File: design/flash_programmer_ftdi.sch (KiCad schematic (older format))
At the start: 13 parts, among them P201 USB_B, U201 FT230X

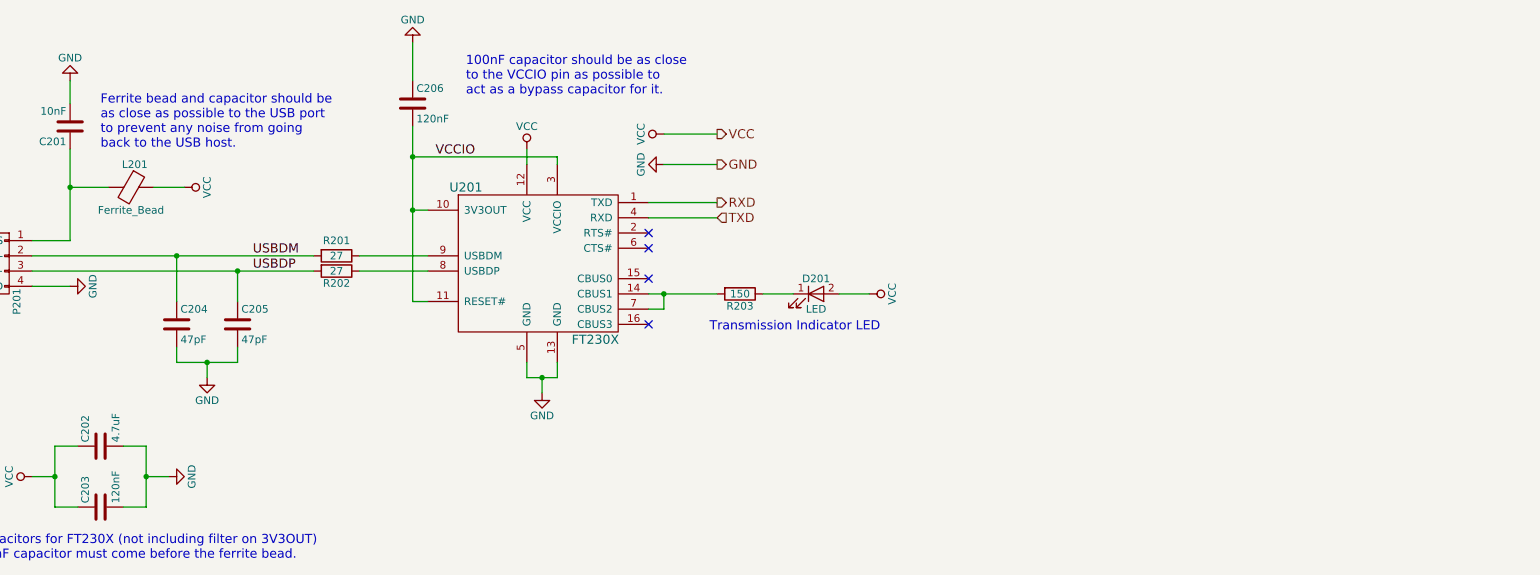
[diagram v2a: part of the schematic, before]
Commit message: Redraw schematic for clarity
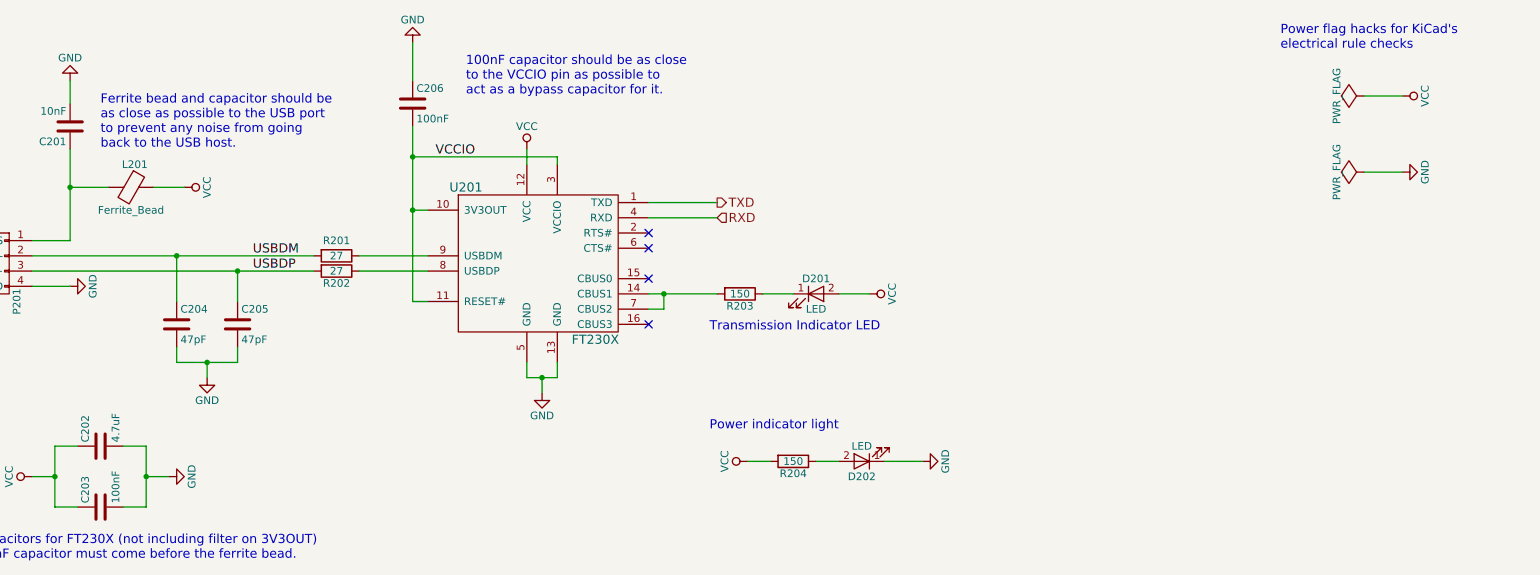
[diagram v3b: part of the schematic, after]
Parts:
- added D202: LED, LEDs:LED_0805, symbol LED
- added R204: 150, Resistors_SMD:R_0805_HandSoldering, symbol R
- C203, C206: value 120nF -> 100nF
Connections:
- net GND: now also D202.1 (K)
- net RXD: now also U201.4 (RXD); no longer U201.1 (TXD)
- net TXD: now also U201.1 (TXD); no longer U201.4 (RXD)
- net VCC: now also R204.2
- new net: D202.2 (A), R204.1
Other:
- note added: "Power flag hacks for KiCad's\nelectrical rule checks"
- note added: "Power indicator light"
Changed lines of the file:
@@
 EESchema Schematic File Version 2
+LIBS:gls27sf010
 LIBS:flash_programmer
 LIBS:power
@@
 $Descr A4 11693 8268
 encoding utf-8
-Sheet 2 3
+Sheet 2 4
 Title ""
 Date ""
@@
 $EndDescr
 $Comp
-L VCC #PWR028
+L VCC #PWR01
 U 1 1 58666138
 P 2500 1700
-F 0 "#PWR028" H 2500 1550 50  0001 C CNN
+F 0 "#PWR01" H 2500 1550 50  0001 C CNN
 F 1 "VCC" H 2500 1850 50  0000 C CNN
 F 2 "" H 2500 1700 50  0000 C CNN
@@
 $EndComp
 $Comp
-L GND #PWR029
+L GND #PWR02
 U 1 1 58666150
 P 1750 1000
-F 0 "#PWR029" H 1750 750 50  0001 C CNN
+F 0 "#PWR02" H 1750 750 50  0001 C CNN
 F 1 "GND" H 1750 850 50  0000 C CNN
 F 2 "" H 1750 1000 50  0000 C CNN
@@
 P 1950 3800
 F 0 "C203" H 1975 3900 50  0000 L CNN
-F 1 "120nF" H 1975 3700 50  0000 L CNN
+F 1 "100nF" H 1975 3700 50  0000 L CNN
 F 2 "Capacitors_SMD:C_0805_HandSoldering" H 1988 3650 50  0001 C CNN
 F 3 "" H 1950 3800 50  0000 C CNN
@@
 P 4000 1150
 F 0 "C206" H 4025 1250 50  0000 L CNN
-F 1 "120nF" H 4025 1050 50  0000 L CNN
+F 1 "100nF" H 4025 1050 50  0000 L CNN
 F 2 "Capacitors_SMD:C_0805_HandSoldering" H 4038 1000 50  0001 C CNN
 F 3 "" H 4000 1150 50  0000 C CNN
@@
 	1650 3400 1800 3400
 $Comp
-L GND #PWR030
+L GND #PWR03
 U 1 1 58666A15
 P 2400 3600
-F 0 "#PWR030" H 2400 3350 50  0001 C CNN
+F 0 "#PWR03" H 2400 3350 50  0001 C CNN
 F 1 "GND" H 2400 3450 50  0000 C CNN
 F 2 "" H 2400 3600 50  0000 C CNN
@@
 $EndComp
 $Comp
-L VCC #PWR031
+L VCC #PWR04
 U 1 1 58666A32
 P 1500 3600
-F 0 "#PWR031" H 1500 3450 50  0001 C CNN
+F 0 "#PWR04" H 1500 3450 50  0001 C CNN
 F 1 "VCC" H 1500 3750 50  0000 C CNN
 F 2 "" H 1500 3600 50  0000 C CNN
@@
 $EndComp
 $Comp
-L GND #PWR032
+L GND #PWR05
 U 1 1 58667B03
 P 4850 3050
-F 0 "#PWR032" H 4850 2800 50  0001 C CNN
+F 0 "#PWR05" H 4850 2800 50  0001 C CNN
 F 1 "GND" H 4850 2900 50  0000 C CNN
 F 2 "" H 4850 3050 50  0000 C CNN
@@
 	2300 1700 2500 1700
 $Comp
-L GND #PWR033
+L GND #PWR06
 U 1 1 58669DB0
 P 1750 2350
-F 0 "#PWR033" H 1750 2100 50  0001 C CNN
+F 0 "#PWR06" H 1750 2100 50  0001 C CNN
 F 1 "GND" H 1750 2200 50  0000 C CNN
 F 2 "" H 1750 2350 50  0000 C CNN
@@
 	4750 1550 4750 1450
 $Comp
-L VCC #PWR034
+L VCC #PWR07
 U 1 1 5867040E
 P 4750 1450
-F 0 "#PWR034" H 4750 1300 50  0001 C CNN
+F 0 "#PWR07" H 4750 1300 50  0001 C CNN
 F 1 "VCC" H 4750 1600 50  0000 C CNN
 F 2 "" H 4750 1450 50  0000 C CNN
@@
 	4000 1000 4000 750
 $Comp
-L GND #PWR035
+L GND #PWR08
 U 1 1 58670F4A
 P 4000 750
-F 0 "#PWR035" H 4000 500 50  0001 C CNN
+F 0 "#PWR08" H 4000 500 50  0001 C CNN
 F 1 "GND" H 4000 600 50  0000 C CNN
 F 2 "" H 4000 750 50  0000 C CNN
@@
 NoConn ~ 5550 2000
 NoConn ~ 5550 2100
-Wire Wire Line
-	5550 1800 6000 1800
-Wire Wire Line
-	5550 1900 6000 1900
 $Comp
 L R R202
@@
 Connection ~ 2650 2850
 $Comp
-L GND #PWR036
+L GND #PWR09
 U 1 1 58674AD8
 P 2650 2950
-F 0 "#PWR036" H 2650 2700 50  0001 C CNN
+F 0 "#PWR09" H 2650 2700 50  0001 C CNN
 F 1 "GND" H 2650 2800 50  0000 C CNN
 F 2 "" H 2650 2950 50  0000 C CNN
@@
 Wire Wire Line
 	6500 2400 6300 2400
+Text HLabel 6000 1900 2    60   Input ~ 0
+RXD
 Text HLabel 6000 1800 2    60   Output ~ 0
-RXD
-Text HLabel 6000 1900 2    60   Input ~ 0
 TXD
-Wire Wire Line
-	5650 1550 6000 1550
-Wire Wire Line
-	5650 1350 6000 1350
-$Comp
-L VCC #PWR037
-U 1 1 5867D289
-P 5650 1350
-F 0 "#PWR037" H 5650 1200 50  0001 C CNN
-F 1 "VCC" H 5650 1500 50  0000 C CNN
-F 2 "" H 5650 1350 50  0000 C CNN
-F 3 "" H 5650 1350 50  0000 C CNN
-	1    5650 1350
-	0    -1   -1   0
-$EndComp
-$Comp
-L GND #PWR038
-U 1 1 5867D436
-P 5650 1550
-F 0 "#PWR038" H 5650 1300 50  0001 C CNN
-F 1 "GND" H 5650 1400 50  0000 C CNN
-F 2 "" H 5650 1550 50  0000 C CNN
-F 3 "" H 5650 1550 50  0000 C CNN
-	1    5650 1550
-	0    1    1    0
-$EndComp
-Text HLabel 6000 1350 2    60   Output ~ 0
-VCC
-Text HLabel 6000 1550 2    60   Output ~ 0
-GND
-$Comp
-L VCC #PWR039
+$Comp
+L VCC #PWR010
 U 1 1 5868E582
 P 7000 2400
-F 0 "#PWR039" H 7000 2250 50  0001 C CNN
+F 0 "#PWR010" H 7000 2250 50  0001 C CNN
 F 1 "VCC" H 7000 2550 50  0000 C CNN
 F 2 "" H 7000 2400 50  0000 C CNN
@@
 $EndComp
 $Comp
-L GND #PWR040
+L GND #PWR011
 U 1 1 588E2AB4
 P 1100 2550
-F 0 "#PWR040" H 1100 2300 50  0001 C CNN
+F 0 "#PWR011" H 1100 2300 50  0001 C CNN
 F 1 "GND" H 1100 2400 50  0000 C CNN
 F 2 "" H 1100 2550 50  0000 C CNN
@@
 	1    0    0    -1
 $EndComp
+$Comp
+L LED D202
+U 1 1 58C28B58
+P 6950 3500
+F 0 "D202" H 6950 3600 50  0000 C CNN
+F 1 "LED" H 6950 3400 50  0000 C CNN
+F 2 "LEDs:LED_0805" H 6950 3500 50  0001 C CNN
+F 3 "" H 6950 3500 50  0000 C CNN
+	1    6950 3500
+	-1   0    0    1
+$EndComp
+$Comp
+L R R204
+U 1 1 58C28B5F
+P 6500 3500
+F 0 "R204" V 6580 3500 50  0000 C CNN
+F 1 "150" V 6500 3500 50  0000 C CNN
+F 2 "Resistors_SMD:R_0805_HandSoldering" V 6430 3500 50  0001 C CNN
+F 3 "" H 6500 3500 50  0000 C CNN
+	1    6500 3500
+	0    1    1    0
+$EndComp
+Wire Wire Line
+	6800 3500 6650 3500
+Wire Wire Line
+	7100 3500 7350 3500
+$Comp
+L GND #PWR012
+U 1 1 58C28B68
+P 7350 3500
+F 0 "#PWR012" H 7350 3250 50  0001 C CNN
+F 1 "GND" H 7350 3350 50  0000 C CNN
+F 2 "" H 7350 3500 50  0000 C CNN
+F 3 "" H 7350 3500 50  0000 C CNN
+	1    7350 3500
+	0    -1   -1   0
+$EndComp
+$Comp
+L VCC #PWR013
+U 1 1 58C28B6E
+P 6200 3500
+F 0 "#PWR013" H 6200 3350 50  0001 C CNN
+F 1 "VCC" H 6200 3650 50  0000 C CNN
+F 2 "" H 6200 3500 50  0000 C CNN
+F 3 "" H 6200 3500 50  0000 C CNN
+	1    6200 3500
+	0    -1   -1   0
+$EndComp
+Wire Wire Line
+	6200 3500 6350 3500
+Text Notes 5950 3300 0    60   ~ 0
+Power indicator light
+Wire Wire Line
+	5550 1800 6000 1800
+Wire Wire Line
+	5550 1900 6000 1900
+$Comp
+L PWR_FLAG #FLG014
+U 1 1 58C31847
+P 10250 1100
+F 0 "#FLG014" H 10250 1195 50  0001 C CNN
+F 1 "PWR_FLAG" H 10250 1280 50  0000 C CNN
+F 2 "" H 10250 1100 50  0000 C CNN
+F 3 "" H 10250 1100 50  0000 C CNN
+	1    10250 1100
+	0    -1   -1   0
+$EndComp
+$Comp
+L VCC #PWR015
+U 1 1 58C31886
+P 10500 1100
+F 0 "#PWR015" H 10500 950 50  0001 C CNN
+F 1 "VCC" H 10500 1250 50  0000 C CNN
+F 2 "" H 10500 1100 50  0000 C CNN
+F 3 "" H 10500 1100 50  0000 C CNN
+	1    10500 1100
+	0    1    1    0
+$EndComp
+$Comp
+L GND #PWR016
+U 1 1 58C318BE
+P 10500 1600
+F 0 "#PWR016" H 10500 1350 50  0001 C CNN
+F 1 "GND" H 10500 1450 50  0000 C CNN
+F 2 "" H 10500 1600 50  0000 C CNN
+F 3 "" H 10500 1600 50  0000 C CNN
+	1    10500 1600
+	0    -1   -1   0
+$EndComp
+$Comp
+L PWR_FLAG #FLG017
+U 1 1 58C3195A
+P 10250 1600
+F 0 "#FLG017" H 10250 1695 50  0001 C CNN
+F 1 "PWR_FLAG" H 10250 1780 50  0000 C CNN
+F 2 "" H 10250 1600 50  0000 C CNN
+F 3 "" H 10250 1600 50  0000 C CNN
+	1    10250 1600
+	0    -1   -1   0
+$EndComp
+Wire Wire Line
+	10250 1100 10500 1100
+Wire Wire Line
+	10250 1600 10500 1600
+Text Notes 9700 800  0    60   ~ 0
+Power flag hacks for KiCad's\nelectrical rule checks
 $EndSCHEMATC

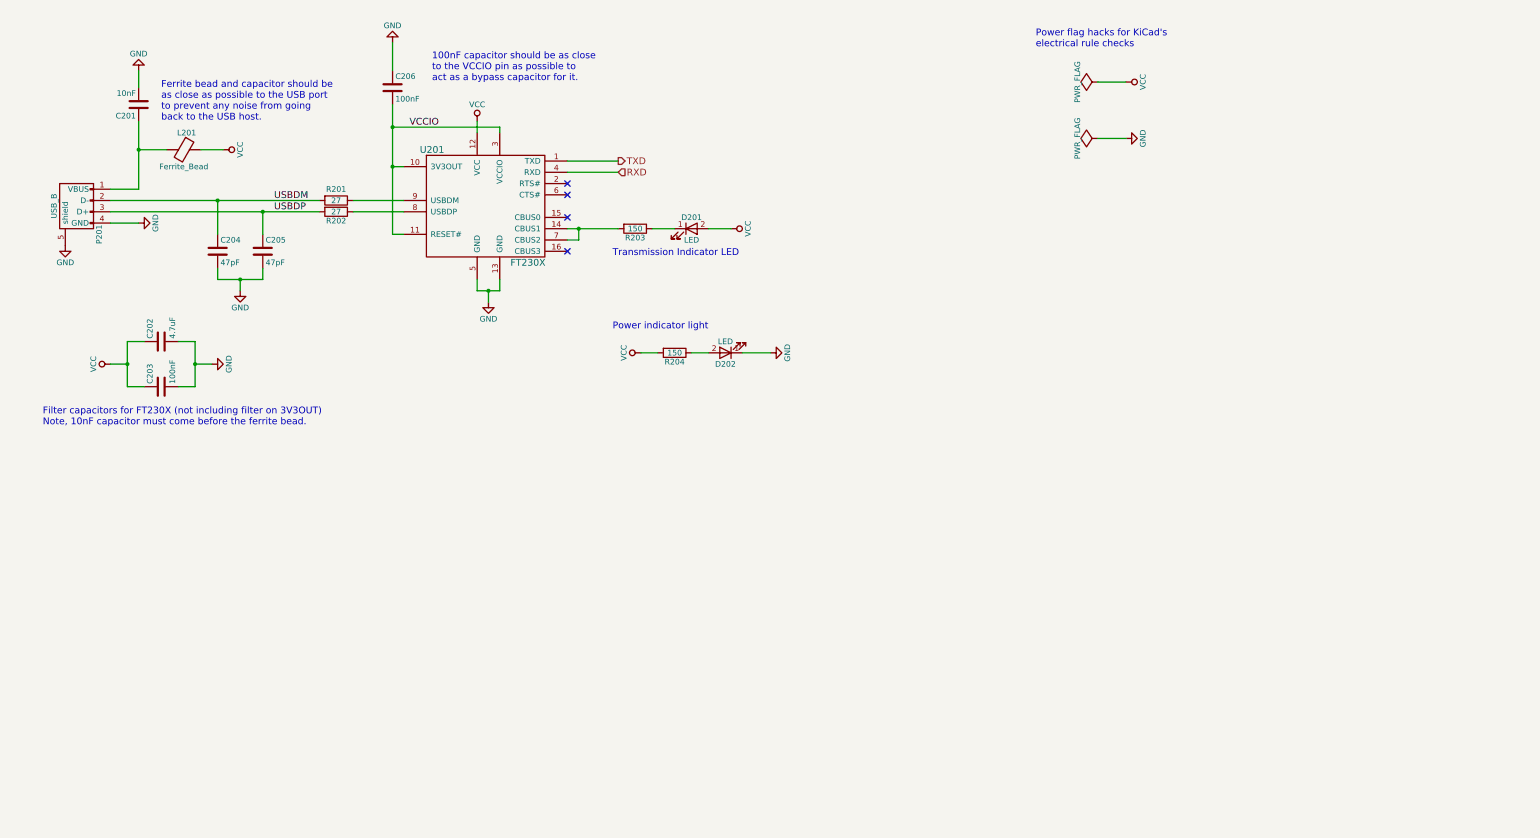
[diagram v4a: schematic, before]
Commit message: Bug fix and more schematic cleanup
The A9_VPP circuit wouldn't work in all cases, so I completely redid it and
it's simpler now.

Also started splitting up the schematic into even more sheets, and sprinkled in
some TODO comments.
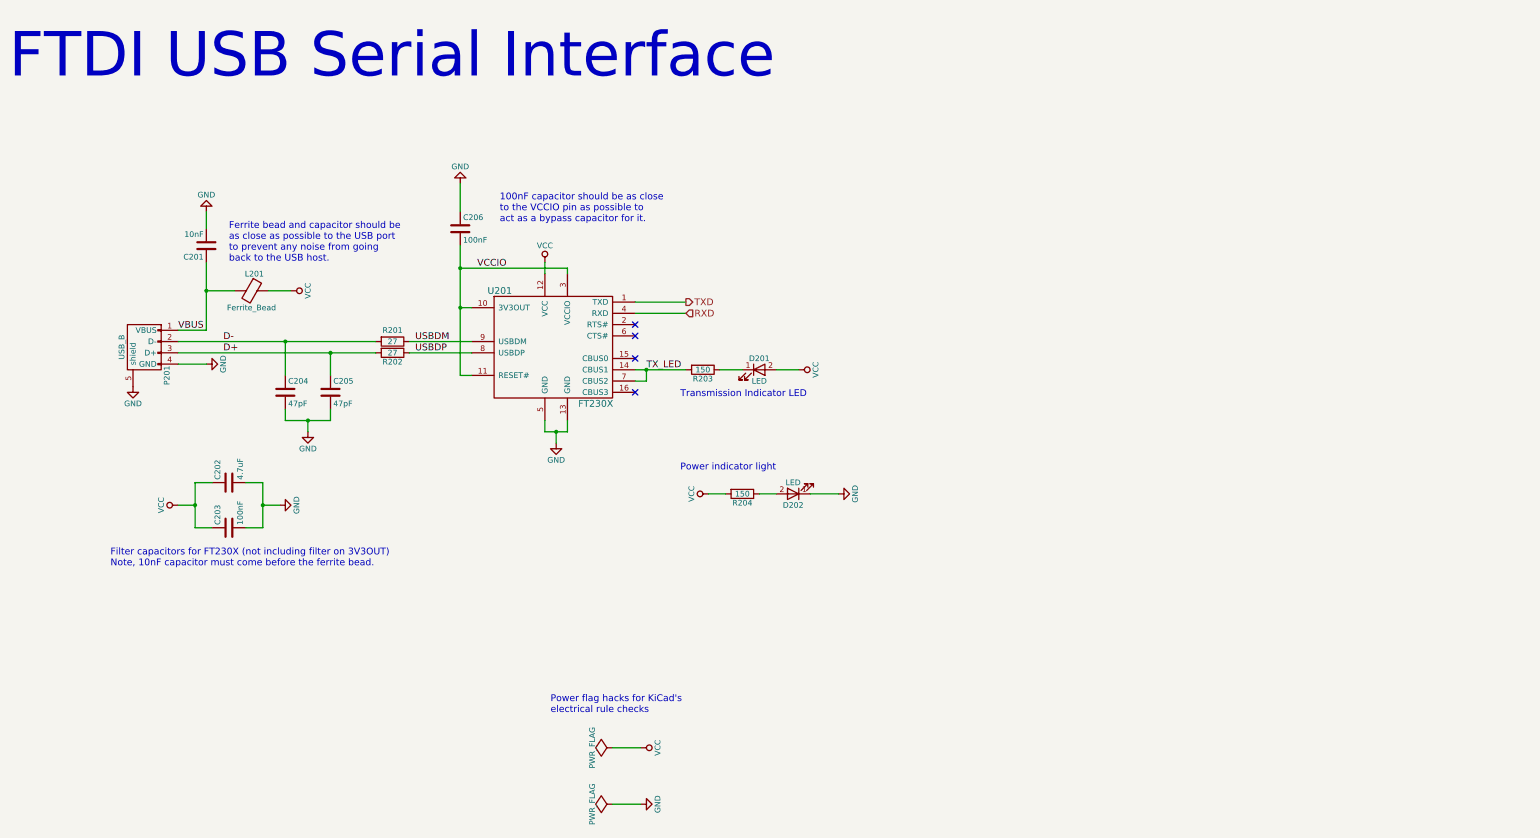
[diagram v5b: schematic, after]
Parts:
- C201, C202, C203, C204, C205, C206, L201: footprint Capacitors_SMD:C_0805_HandSoldering -> Resistors_SMD:R_0805_HandSoldering
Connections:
- net USBDM: now also R201.1, U201.9 (USBDM); no longer C204.1, P201.2 (D-), R201.2
- net USBDP: now also R202.1, U201.8 (USBDP); no longer C205.1, P201.3 (D+), R202.2
- net VBUS: now reaches C201.1, L201.2, P201.1 (VBUS)
- net TX_LED: now reaches R203.2, U201.14 (CBUS1), U201.7 (CBUS2)
- new net D+: C205.1, P201.3 (D+), R202.2
- new net D-: C204.1, P201.2 (D-), R201.2
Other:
- note added: "FTDI USB Serial Interface"
- moved on the sheet: C201, C202, C203, C204, C205, C206, D201, D202, L201, P201, R201, R202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

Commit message: More schematic clean up
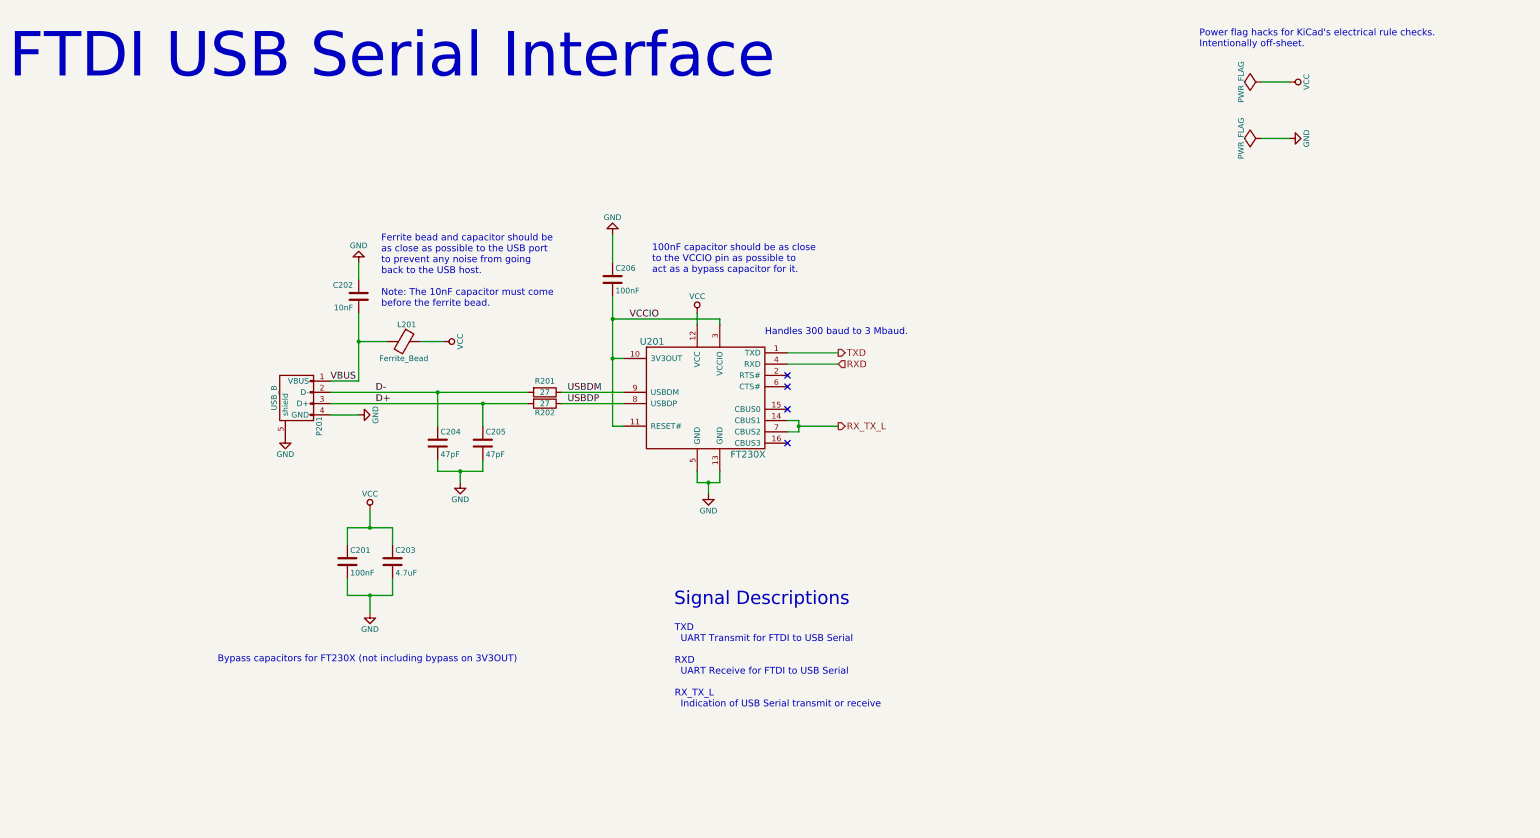
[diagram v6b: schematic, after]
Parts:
- removed D201, D202: LED, LEDs:LED_0805, symbol LED
- removed R203, R204: 150, Resistors_SMD:R_0805_HandSoldering, symbol R
- C201: renamed from C203; footprint Resistors_SMD:R_0805_HandSoldering -> Resistors_SMD:R_0603_HandSoldering
- C202: renamed from C201; footprint Resistors_SMD:R_0805_HandSoldering -> Resistors_SMD:R_0603_HandSoldering
- C204, C205, C206, R201, R202: footprint Resistors_SMD:R_0805_HandSoldering -> Resistors_SMD:R_0603_HandSoldering
- renumbered C202 to C203
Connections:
- net TX_LED renamed RX_TX_L
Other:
- note added: "Bypass capacitors for FT230X (not including bypass on 3V3OUT)"
- note added: "Ferrite bead and capacitor should be\nas close as possible to the USB port\nto prevent any noise from going\nback to the USB host.\n\nNote: The 10nF capacitor must come\nbefore the ferrite bead."
- note added: "Handles 300 baud to 3 Mbaud."
- note added: "Power flag hacks for KiCad's electrical rule checks.\nIntentionally off-sheet."
- note added: "Signal Descriptions"
- note added: "TXD\n UART Transmit for FTDI to USB Serial\n\nRXD\n UART Receive for FTDI to USB Serial\n\nRX_TX_L\n Indication of USB Serial transmit or receive"
- note removed: "Ferrite bead and capacitor should be\nas close as possible to the USB port\nto prevent any noise from going\nback to the USB host."
- note removed: "Filter capacitors for FT230X (not including filter on 3V3OUT)\nNote, 10nF capacitor must come before the ferrite bead."
- note removed: "Power flag hacks for KiCad's\nelectrical rule checks"
- note removed: "Power indicator light"
- note removed: "Transmission Indicator LED"
- moved on the sheet: C201, C202, C203, C204, C205, C206, L201, P201, R201, R202, U201
